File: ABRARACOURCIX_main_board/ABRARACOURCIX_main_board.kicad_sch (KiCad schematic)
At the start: 1 part, among them U1 STM32F469VGTx

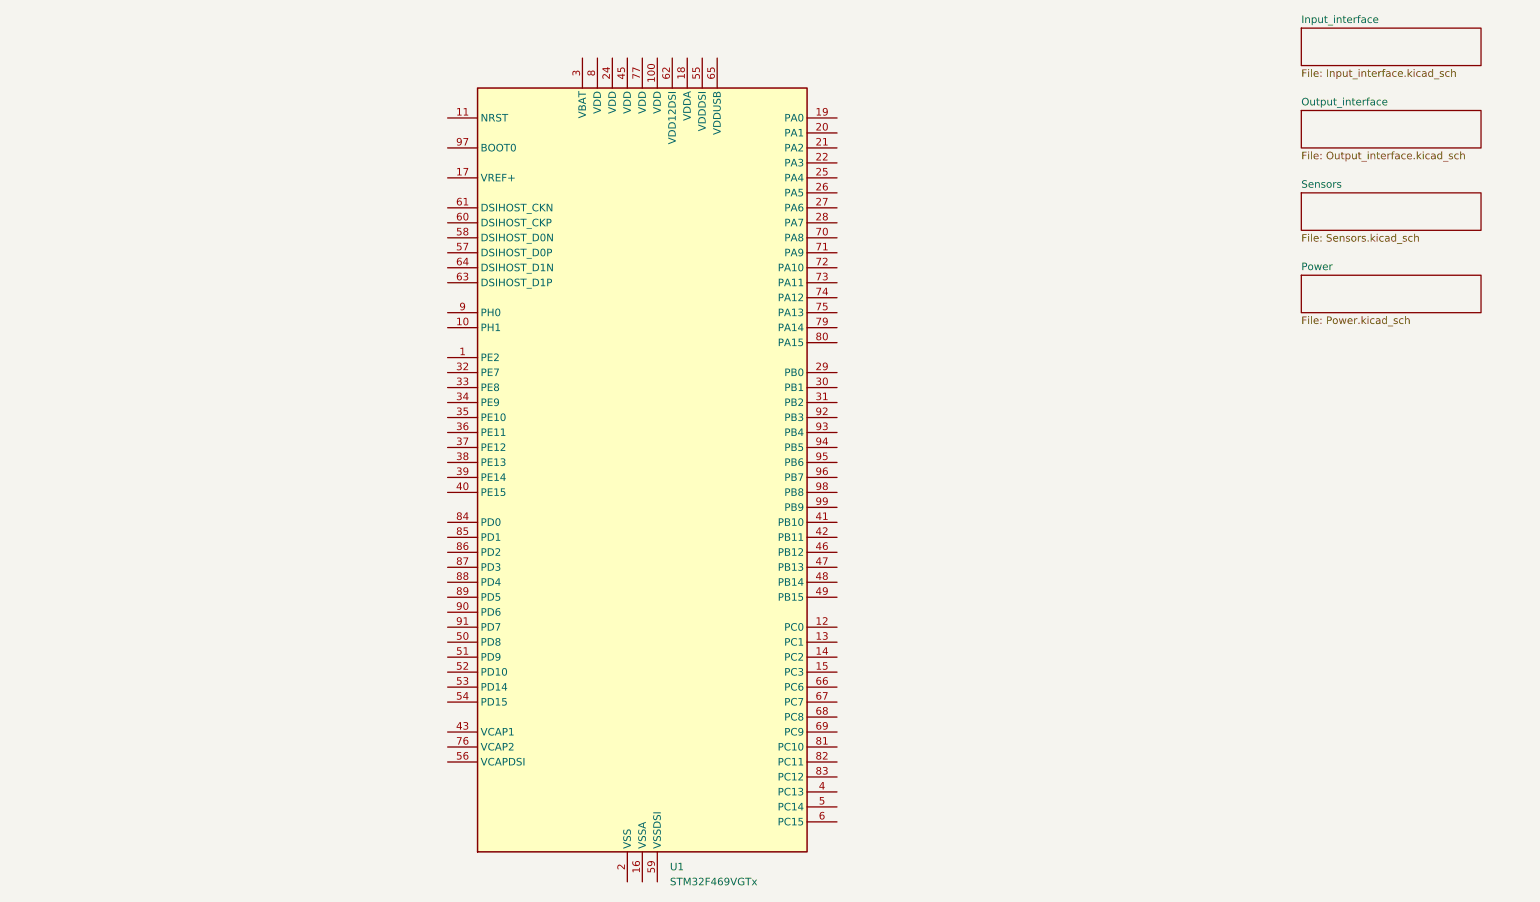
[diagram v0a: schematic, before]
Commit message: Avancement
Decoupling caps
Changement de stm32
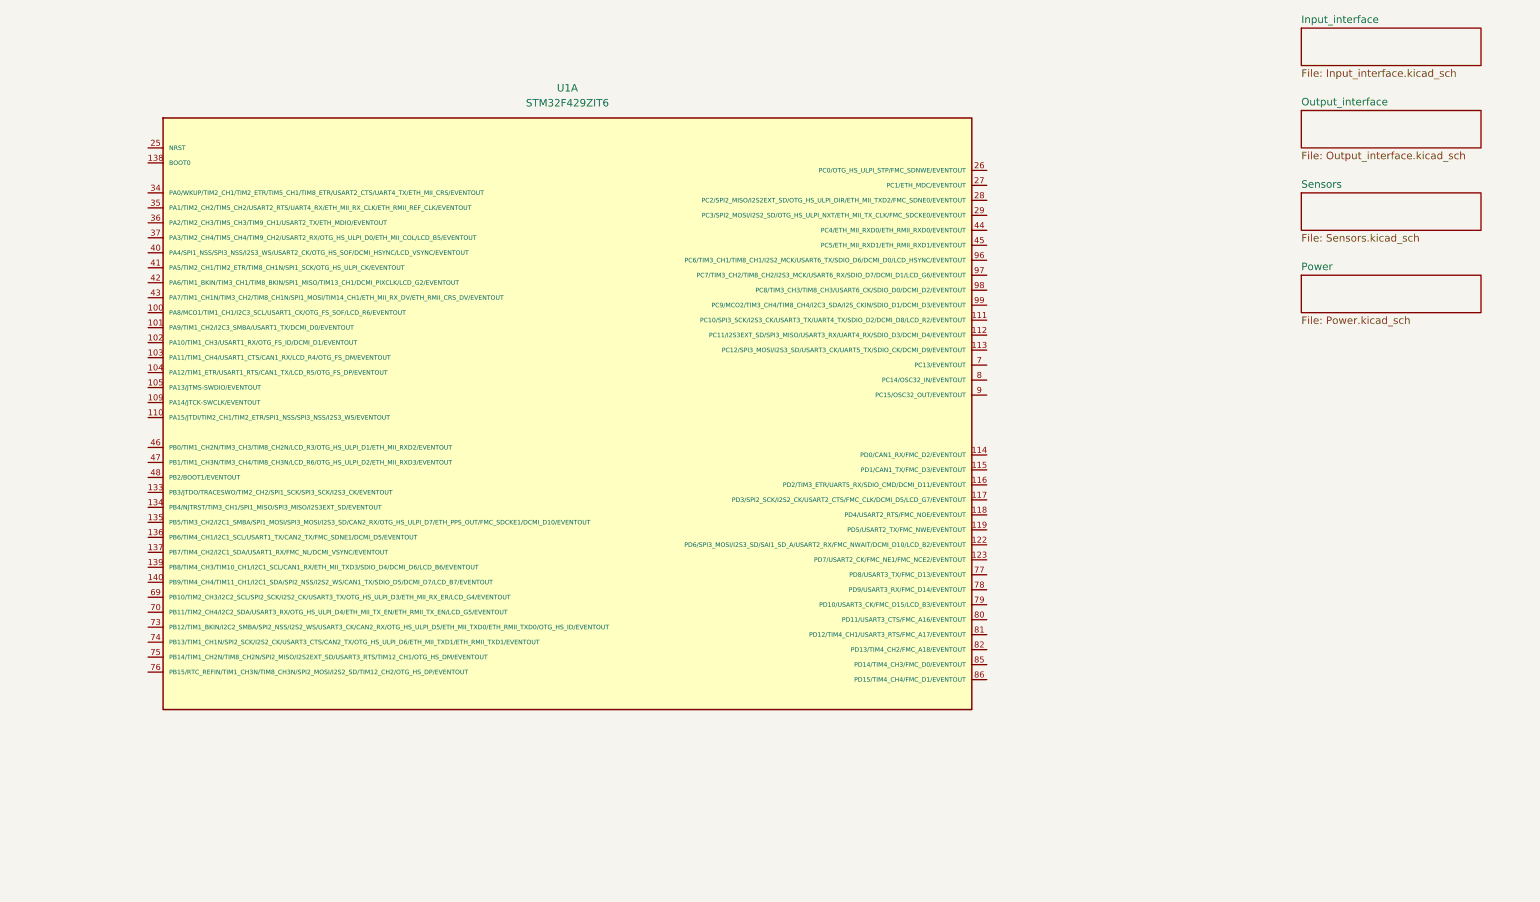
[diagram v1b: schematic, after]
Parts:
- removed U1: STM32F469VGTx, Package_QFP:LQFP-100_14x14mm_P0.5mm, symbol MCU_ST_STM32F4:STM32F469VGTx
- added U1: STM32F429ZIT6, STM32F429ZIT6:QFP50P2200X2200X160-144N, symbol GAUL_ABRARACOURCIX:STM32F429ZIT6

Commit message: Avancement
Commencer à relier le stm32
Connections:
- net UART_CTS: now reaches U1.117 (PD3/SPI2_SCK/I2S2_CK/USART2_CTS/FMC_CLK/DCMI_D5/LCD_G7/EVENTOUT)
- net UART_RTS: now reaches U1.118 (PD4/USART2_RTS/FMC_NOE/EVENTOUT)
- net UART2_BT_RX: now reaches U1.119 (PD5/USART2_TX/FMC_NWE/EVENTOUT)
- net UART2_BT_TX: now reaches U1.122 (PD6/SPI3_MOSI/I2S3_SD/SAI1_SD_A/USART2_RX/FMC_NWAIT/DCMI_D10/LCD_B2/EVENTOUT)
- net BT_Config/Run: now reaches U1.26 (PC0/OTG_HS_ULPI_STP/FMC_SDNWE/EVENTOUT)
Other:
- note added: "Inversion RX/TX au MCU"
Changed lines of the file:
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@@
 	(generator_version "9.0")
 	(paper "A4")
+	(arc
+		(start 205.74 102.87)
+		(mid 206.7921 105.41)
+		(end 205.74 107.95)
+		(stroke
+			(width 0)
+			(type default)
+		)
+		(fill
+			(type none)
+		)
+	)
+	(text "Inversion RX/TX\nau MCU"
+		(exclude_from_sim no)
+		(at 215.9 105.664 0)
+		(effects
+			(font
+				(size 1.27 1.27)
+			)
+		)
+	)
+	(wire
+		(pts
+			(xy 190.5 99.06) (xy 194.31 99.06)
+		)
+		(stroke
+			(width 0)
+			(type default)
+		)
+	)
+	(wire
+		(pts
+			(xy 193.04 43.18) (xy 190.5 43.18)
+		)
+		(stroke
+			(width 0)
+			(type default)
+		)
+	)
+	(wire
+		(pts
+			(xy 190.5 101.6) (xy 194.31 101.6)
+		)
+		(stroke
+			(width 0)
+			(type default)
+		)
+	)
+	(global_label "UART2_BT_RX"
+		(shape input)
+		(at 190.5 104.14 0)
+		(fields_autoplaced yes)
+		(effects
+			(font
+				(size 1.27 1.27)
+			)
+			(justify left)
+		)
+		(property "Intersheetrefs" "${INTERSHEET_REFS}"
+			(at 206.0037 104.14 0)
+			(effects
+				(font
+					(size 1.27 1.27)
+				)
+				(justify left)
+				(hide yes)
+			)
+		)
+	)
+	(global_label "UART2_BT_TX"
+		(shape input)
+		(at 190.5 106.68 0)
+		(fields_autoplaced yes)
+		(effects
+			(font
+				(size 1.27 1.27)
+			)
+			(justify left)
+		)
+		(property "Intersheetrefs" "${INTERSHEET_REFS}"
+			(at 205.7013 106.68 0)
+			(effects
+				(font
+					(size 1.27 1.27)
+				)
+				(justify left)
+				(hide yes)
+			)
+		)
+	)
+	(global_label "UART_CTS"
+		(shape input)
+		(at 194.31 99.06 0)
+		(fields_autoplaced yes)
+		(effects
+			(font
+				(size 1.27 1.27)
+			)
+			(justify left)
+		)
+		(property "Intersheetrefs" "${INTERSHEET_REFS}"
+			(at 206.3666 99.06 0)
+			(effects
+				(font
+					(size 1.27 1.27)
+				)
+				(justify left)
+				(hide yes)
+			)
+		)
+	)
+	(global_label "UART_RTS"
+		(shape input)
+		(at 194.31 101.6 0)
+		(fields_autoplaced yes)
+		(effects
+			(font
+				(size 1.27 1.27)
+			)
+			(justify left)
+		)
+		(property "Intersheetrefs" "${INTERSHEET_REFS}"
+			(at 206.3666 101.6 0)
+			(effects
+				(font
+					(size 1.27 1.27)
+				)
+				(justify left)
+				(hide yes)
+			)
+		)
+	)
+	(global_label "BT_Config{slash}Run"
+		(shape input)
+		(at 193.04 43.18 0)
+		(fields_autoplaced yes)
+		(effects
+			(font
+				(size 1.27 1.27)
+			)
+			(justify left)
+		)
+		(property "Intersheetrefs" "${INTERSHEET_REFS}"
+			(at 210.1764 43.18 0)
+			(effects
+				(font
+					(size 1.27 1.27)
+				)
+				(justify left)
+				(hide yes)
+			)
+		)
+	)
 	(symbol
 		(lib_id "GAUL_ABRARACOURCIX:STM32F429ZIT6")

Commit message: Reprise de contrôle
Schematics terminés
Reste à associer des composantes et vérification
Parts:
- added D3: 599-0410-127F, symbol Device:LED
- added R2: 40, symbol Device:R
- added TP1, TP2, TP3: TestPoint, symbol Connector:TestPoint
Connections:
- net SYS_SWDIO: now reaches U1.105 (PA13/JTMS-SWDIO/EVENTOUT)
- net SYS_SWCLK: now reaches U1.109 (PA14/JTCK-SWCLK/EVENTOUT)
- net PWM_Moteur: now reaches U1.134 (PB4/NJTRST/TIM3_CH1/SPI1_MISO/SPI3_MISO/I2S3EXT_SD/EVENTOUT)
- net PWM_Moteur: now also TP3.1
- net BNO_RESET: now reaches U1.135 (PB5/TIM3_CH2/I2C1_SMBA/SPI1_MOSI/SPI3_MOSI/I2S3_SD/CAN2_RX/OTG_HS_ULPI_D7/ETH_PPS_OUT/FMC_SDCKE1/DCMI_D10/EVENTOUT)
- net SCL: now reaches U1.136 (PB6/TIM4_CH1/I2C1_SCL/USART1_TX/CAN2_TX/FMC_SDNE1/DCMI_D5/EVENTOUT)
- net SDA: now reaches U1.137 (PB7/TIM4_CH2/I2C1_SDA/USART1_RX/FMC_NL/DCMI_VSYNC/EVENTOUT)
- net BNO_BOOT: now reaches U1.139 (PB8/TIM4_CH3/TIM10_CH1/I2C1_SCL/CAN1_RX/ETH_MII_TXD3/SDIO_D4/DCMI_D6/LCD_B6/EVENTOUT)
- net BNO_INT_OUT: now reaches U1.140 (PB9/TIM4_CH4/TIM11_CH1/I2C1_SDA/SPI2_NSS/I2S2_WS/CAN1_TX/SDIO_D5/DCMI_D7/LCD_B7/EVENTOUT)
- net NRST: now reaches U1.25 (NRST)
- net at U1.27 (PC1/ETH_MDC/EVENTOUT): now also R2.1
- net BUZZER_IB: now reaches U1.36 (PA2/TIM2_CH3/TIM5_CH3/TIM9_CH1/USART2_TX/ETH_MDIO/EVENTOUT)
- net VIout_sense: now reaches U1.46 (PB0/TIM1_CH2N/TIM3_CH3/TIM8_CH2N/LCD_R3/OTG_HS_ULPI_D1/ETH_MII_RXD2/EVENTOUT)
- net VBAT_ADC: now reaches U1.47 (PB1/TIM1_CH3N/TIM3_CH4/TIM8_CH3N/LCD_R6/OTG_HS_ULPI_D2/ETH_MII_RXD3/EVENTOUT)
- net PWM_Servo_1: now reaches U1.81 (PD12/TIM4_CH1/USART3_RTS/FMC_A17/EVENTOUT)
- net PWM_Servo_2: now reaches U1.82 (PD13/TIM4_CH2/FMC_A18/EVENTOUT)
- net PWM_Servo_3: now reaches U1.85 (PD14/TIM4_CH3/FMC_D0/EVENTOUT)
- net PWM_Servo_4: now reaches U1.86 (PD15/TIM4_CH4/FMC_D1/EVENTOUT)
- net UART2_BT_RX renamed HC_RX
- net HC_RX: now also TP1.1
- net UART2_BT_TX renamed HC_TX
- net HC_TX: now also TP2.1
- net UART_CTS: no longer names the net of U1.117 (PD3/SPI2_SCK/I2S2_CK/USART2_CTS/FMC_CLK/DCMI_D5/LCD_G7/EVENTOUT)
- net UART_RTS: no longer names the net of U1.118 (PD4/USART2_RTS/FMC_NOE/EVENTOUT)
- new net: D3.2 (A), R2.2
- new net GND: D3.1 (K)
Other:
- note added: "LED rouge Debug VLED = 2.1V à 30 mA R= (3.3-2.1)/30mA = 40 Ohm"

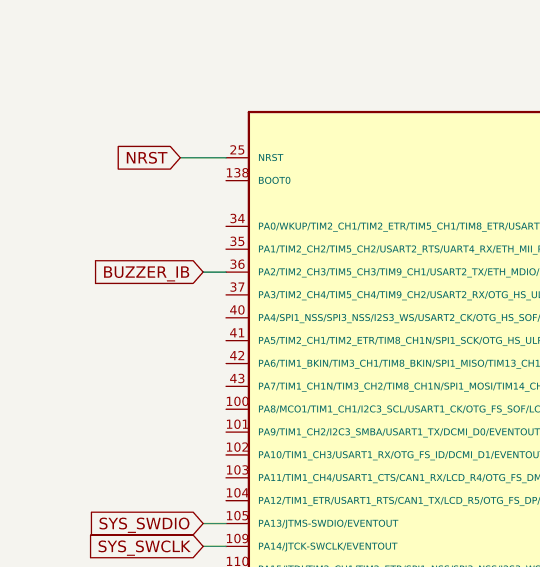
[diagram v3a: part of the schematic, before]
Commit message: Assignation d<empreintes terminée
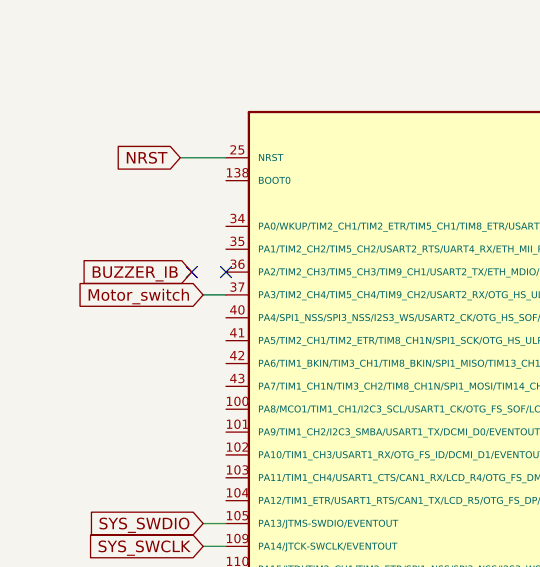
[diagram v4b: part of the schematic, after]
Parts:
- D3: footprint (none) -> Diode_SMD:D_1206_3216Metric_Pad1.42x1.75mm_HandSolder
- R2: footprint (none) -> Resistor_SMD:R_1206_3216Metric_Pad1.30x1.75mm_HandSolder
- TP1, TP2, TP3: footprint (none) -> TestPoint:TestPoint_THTPad_2.0x2.0mm_Drill1.0mm
- U1: footprint STM32F429ZIT6:QFP50P2200X2200X160-144N -> Librairie_footprint:QFP50P2200X2200X160-144N
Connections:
- net BUZZER_IB: no longer U1.36 (PA2/TIM2_CH3/TIM5_CH3/TIM9_CH1/USART2_TX/ETH_MDIO/EVENTOUT)
- net Motor_switch: now reaches U1.37 (PA3/TIM2_CH4/TIM5_CH4/TIM9_CH2/USART2_RX/OTG_HS_ULPI_D0/ETH_MII_COL/LCD_B5/EVENTOUT)
- no-connect marks 0 -> 2
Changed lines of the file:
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@@
 		(color 0 0 0 0)
 	)
+	(no_connect
+		(at 48.26 52.07)
+	)
+	(no_connect
+		(at 44.45 52.07)
+	)
 	(wire
 		(pts
@@
 	(wire
 		(pts
+			(xy 45.72 54.61) (xy 48.26 54.61)
+		)
+		(stroke
+			(width 0)
+			(type default)
+		)
+	)
+	(wire
+		(pts
 			(xy 193.04 127) (xy 190.5 127)
 		)
@@
 	(wire
 		(pts
-			(xy 45.72 52.07) (xy 48.26 52.07)
-		)
-		(stroke
-			(width 0)
-			(type default)
-		)
-	)
-	(wire
-		(pts
 			(xy 44.45 92.71) (xy 48.26 92.71)
 		)
@@
 		)
 	)
+	(global_label "Motor_switch"
+		(shape input)
+		(at 45.72 54.61 180)
+		(fields_autoplaced yes)
+		(effects
+			(font
+				(size 1.27 1.27)
+			)
+			(justify right)
+		)
+		(property "Intersheetrefs" "${INTERSHEET_REFS}"
+			(at 30.5792 54.61 0)
+			(effects
+				(font
+					(size 1.27 1.27)
+				)
+				(justify right)
+				(hide yes)
+			)
+		)
+	)
 	(global_label "SYS_SWDIO"
 		(shape input)
@@
 	(global_label "BUZZER_IB"
 		(shape input)
-		(at 45.72 52.07 180)
+		(at 44.45 52.07 180)
 		(fields_autoplaced yes)
 		(effects
@@
 		)
 		(property "Intersheetrefs" "${INTERSHEET_REFS}"
-			(at 32.4539 52.07 0)
+			(at 31.1839 52.07 0)
 			(effects
 				(font
@@
 			)
 		)
-		(property "Footprint" ""
+		(property "Footprint" "TestPoint:TestPoint_THTPad_2.0x2.0mm_Drill1.0mm"
 			(at 189.23 106.68 0)
 			(effects
@@
 			)
 		)
-		(property "Footprint" ""
+		(property "Footprint" "Resistor_SMD:R_1206_3216Metric_Pad1.30x1.75mm_HandSolder"
 			(at 209.042 49.53 90)
 			(effects
@@
 			)
 		)
-		(property "Footprint" "STM32F429ZIT6:QFP50P2200X2200X160-144N"
+		(property "Footprint" "Librairie_footprint:QFP50P2200X2200X160-144N"
 			(at 124.46 125.73 0)
 			(effects
@@
 			)
 		)
-		(property "Footprint" ""
+		(property "Footprint" "TestPoint:TestPoint_THTPad_2.0x2.0mm_Drill1.0mm"
 			(at 39.37 100.33 0)
 			(effects
@@
 			)
 		)
-		(property "Footprint" ""
+		(property "Footprint" "TestPoint:TestPoint_THTPad_2.0x2.0mm_Drill1.0mm"
 			(at 199.39 104.14 0)
 			(effects
@@
 			)
 		)
-		(property "Footprint" ""
+		(property "Footprint" "Diode_SMD:D_1206_3216Metric_Pad1.42x1.75mm_HandSolder"
 			(at 210.82 57.15 0)
 			(effects
